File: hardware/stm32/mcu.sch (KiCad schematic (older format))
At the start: 13 parts, among them J1 LCD, J2 SD Card, J3 Radio, J4 Inside, J5 Outside, U1 PC817, U3 bluepill, U4 PC817

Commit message: bluepill Schematics 0.99
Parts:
- removed R3: R_Small, Resistors_SMD:R_0603_HandSoldering, symbol R_Small
- added C10, C4, C5, C6, C7: 100n, Capacitors_SMD:C_0805, symbol C_Small
- added C11, C8, C9: 10u, Capacitors_Tantalum_SMD:CP_Tantalum_Case-A_EIA-3216-18_Reflow, symbol CP_Small
- added J15: Screw_Terminal_01x02, TerminalBlock:TerminalBlock_bornier-2_P5.08mm, symbol Screw_Terminal_01x02
- added J16: Conn_01x02_Male, Pin_Headers:Pin_Header_Straight_1x02_Pitch2.54mm, symbol Conn_01x02_Male
- added J17: ESP-01, Socket_Strips:Socket_Strip_Straight_2x04_Pitch2.54mm, symbol Conn_02x04_Odd_Even
- added J18: USART1, Pin_Headers:Pin_Header_Straight_1x04_Pitch2.54mm, symbol Conn_01x04
- added J19: Buttons, Pin_Headers:Pin_Header_Straight_1x05_Pitch2.54mm, symbol Conn_01x05
- added R10, R11, R12, R6, R7, R8, R9: 470, Resistors_SMD:R_0603_HandSoldering, symbol R_Small
- added U12: LM1117-3.3, TO_SOT_Packages_SMD:SOT-223, symbol LM1117-3.3
- R1, R2: value R_Small -> 4.7k
- R4, R5: value R_Small -> 470
- U1, U4: footprint Housings_SSOP:SOP-4_3.8x4.1mm_Pitch2.54mm -> Housings_DIP:DIP-4_W7.62mm_LongPads
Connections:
- net +3V3: now also J2.6 (Pin_6), C10.1, C11.1, C7.1, C9.1, J17.3 (Pin_3), J17.4 (Pin_4), J17.5 (Pin_5), J17.6 (Pin_6), J17.8 (Pin_8), J18.4 (Pin_4), U12.2 (VO), U12.4 (VO)
- net +5V: now also C4.1, C5.1, C6.1, C8.1, J15.1 (Pin_1), J16.2 (Pin_2), U12.3 (VI); no longer J2.6 (Pin_6), U3.18 (5V)
- net GND: now also C10.2, C11.2, C4.2, C5.2, C6.2, C7.2, C8.2, C9.2, J15.2 (Pin_2), J17.1 (Pin_1), J18.1 (Pin_1), J19.5 (Pin_5), U12.1 (GND/ADJ)
- net IG: now also R12.2; no longer U3.25 (PA0)
- net IR: now also R10.2; no longer U3.27 (PA2)
- net IY: now also R11.2; no longer U3.26 (PA1)
- net LOOP_I: now also U3.4 (PB15); no longer U3.35 (PB10)
- net LOOP_O: now also U3.3 (PB14); no longer U3.36 (PB11)
- net OG: now also R9.2; no longer U3.28 (PA3)
- net OR: now also R7.2; no longer U3.34 (PB1)
- net OY: now also R8.2; no longer U3.33 (PB0)
- net at U3.1 (PB12): now also R6.2
- net BTN4: now reaches U3.10 (PA15)
- net BTN4: now also J19.4 (Pin_4)
- net TX1: now reaches U3.14 (PB6)
- net TX1: now also J18.3 (Pin_3)
- net RX1: now reaches U3.15 (PB7)
- net RX1: now also J18.2 (Pin_2)
- net BTN1: now reaches U3.7 (PA10)
- net BTN1: now also J19.1 (Pin_1)
- net BTN2: now reaches U3.8 (PA11)
- net BTN2: now also J19.2 (Pin_2)
- net BTN3: now reaches U3.9 (PA12)
- net BTN3: now also J19.3 (Pin_3)
- new net: J16.1 (Pin_1), U3.18 (5V)
- new net: R12.1, U3.25 (PA0)
- new net: R11.1, U3.26 (PA1)
- new net: R10.1, U3.27 (PA2)
- new net: R9.1, U3.28 (PA3)
- new net: R8.1, U3.33 (PB0)
- new net: R7.1, U3.34 (PB1)
- new net ESP_RX: J17.7 (Pin_7), U3.35 (PB10)
- new net ESP_TX: J17.2 (Pin_2), U3.36 (PB11)
- new net OPEN: R6.1
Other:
- moved on the sheet: J2

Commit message: bluepill PCB progress
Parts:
- added C12, C13: 100n, Capacitors_SMD:C_0805, symbol C_Small
- J15: value Screw_Terminal_01x02 -> +5V
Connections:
- net +3V3: now also C12.1, C13.1
- net +5V: now also J15.2 (Pin_2); no longer J15.1 (Pin_1)
- net GND: now also J15.1 (Pin_1), C12.2, C13.2; no longer J15.2 (Pin_2)
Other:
- moved on the sheet: C11, C9
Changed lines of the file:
@@
 $EndComp
 $Comp
-L +3.3V #PWR15
+L +3.3V #PWR09
 U 1 1 5A5F315E
 P 4600 2650
-F 0 "#PWR15" H 4600 2500 50  0001 C CNN
+F 0 "#PWR09" H 4600 2500 50  0001 C CNN
 F 1 "+3.3V" H 4600 2790 50  0000 C CNN
 F 2 "" H 4600 2650 50  0001 C CNN
@@
 $EndComp
 $Comp
-L GND #PWR18
+L GND #PWR010
 U 1 1 5A5F3165
 P 4700 5050
-F 0 "#PWR18" H 4700 4800 50  0001 C CNN
+F 0 "#PWR010" H 4700 4800 50  0001 C CNN
 F 1 "GND" H 4700 4900 50  0000 C CNN
 F 2 "" H 4700 5050 50  0001 C CNN
@@
 $EndComp
 $Comp
-L +3.3V #PWR19
+L +3.3V #PWR011
 U 1 1 5A5F316F
 P 6150 2650
-F 0 "#PWR19" H 6150 2500 50  0001 C CNN
+F 0 "#PWR011" H 6150 2500 50  0001 C CNN
 F 1 "+3.3V" H 6150 2790 50  0000 C CNN
 F 2 "" H 6150 2650 50  0001 C CNN
@@
 $EndComp
 $Comp
-L GND #PWR20
+L GND #PWR012
 U 1 1 5A5F317B
 P 6200 5050
-F 0 "#PWR20" H 6200 4800 50  0001 C CNN
+F 0 "#PWR012" H 6200 4800 50  0001 C CNN
 F 1 "GND" H 6200 4900 50  0000 C CNN
 F 2 "" H 6200 5050 50  0001 C CNN
@@
 $EndComp
 $Comp
-L +5V #PWR14
+L +5V #PWR013
 U 1 1 5A5F3181
 P 4500 4050
-F 0 "#PWR14" H 4500 3900 50  0001 C CNN
+F 0 "#PWR013" H 4500 3900 50  0001 C CNN
 F 1 "+5V" H 4500 4190 50  0000 C CNN
 F 2 "" H 4500 4050 50  0001 C CNN
@@
 $EndComp
 $Comp
-L GND #PWR12
+L GND #PWR014
 U 1 1 5A5F4705
 P 3850 5050
-F 0 "#PWR12" H 3850 4800 50  0001 C CNN
+F 0 "#PWR014" H 3850 4800 50  0001 C CNN
 F 1 "GND" H 3850 4900 50  0000 C CNN
 F 2 "" H 3850 5050 50  0001 C CNN
@@
 $EndComp
 $Comp
-L +5V #PWR11
+L +5V #PWR015
 U 1 1 5A5F5C21
 P 3850 2650
-F 0 "#PWR11" H 3850 2500 50  0001 C CNN
+F 0 "#PWR015" H 3850 2500 50  0001 C CNN
 F 1 "+5V" H 3850 2790 50  0000 C CNN
 F 2 "" H 3850 2650 50  0001 C CNN
@@
 CS
 $Comp
-L GND #PWR22
+L GND #PWR016
 U 1 1 5A5F62DE
 P 7050 3650
-F 0 "#PWR22" H 7050 3400 50  0001 C CNN
+F 0 "#PWR016" H 7050 3400 50  0001 C CNN
 F 1 "GND" H 7050 3500 50  0000 C CNN
 F 2 "" H 7050 3650 50  0001 C CNN
@@
 $EndComp
 $Comp
-L GND #PWR30
+L GND #PWR017
 U 1 1 5A5F7A2A
 P 9050 3700
-F 0 "#PWR30" H 9050 3450 50  0001 C CNN
+F 0 "#PWR017" H 9050 3450 50  0001 C CNN
 F 1 "GND" H 9050 3550 50  0000 C CNN
 F 2 "" H 9050 3700 50  0001 C CNN
@@
 $EndComp
 $Comp
-L +3.3V #PWR24
+L +3.3V #PWR018
 U 1 1 5A5F7B0F
 P 8000 2700
-F 0 "#PWR24" H 8000 2550 50  0001 C CNN
+F 0 "#PWR018" H 8000 2550 50  0001 C CNN
 F 1 "+3.3V" H 8000 2840 50  0000 C CNN
 F 2 "" H 8000 2700 50  0001 C CNN
@@
 Connection ~ 3250 1700
 $Comp
-L +5V #PWR9
+L +5V #PWR019
 U 1 1 5A60590D
 P 3250 1600
-F 0 "#PWR9" H 3250 1450 50  0001 C CNN
+F 0 "#PWR019" H 3250 1450 50  0001 C CNN
 F 1 "+5V" H 3250 1740 50  0000 C CNN
 F 2 "" H 3250 1600 50  0001 C CNN
@@
 $EndComp
 $Comp
-L +3.3V #PWR16
+L +3.3V #PWR020
 U 1 1 5A605990
 P 4700 1600
-F 0 "#PWR16" H 4700 1450 50  0001 C CNN
+F 0 "#PWR020" H 4700 1450 50  0001 C CNN
 F 1 "+3.3V" H 4700 1740 50  0000 C CNN
 F 2 "" H 4700 1600 50  0001 C CNN
@@
 $EndComp
 $Comp
-L GND #PWR10
+L GND #PWR021
 U 1 1 5A6059E3
 P 3250 2100
-F 0 "#PWR10" H 3250 1850 50  0001 C CNN
+F 0 "#PWR021" H 3250 1850 50  0001 C CNN
 F 1 "GND" H 3250 1950 50  0000 C CNN
 F 2 "" H 3250 2100 50  0001 C CNN
@@
 L Screw_Terminal_01x02 J15
 U 1 1 5A606802
-P 2600 1800
-F 0 "J15" H 2600 1900 50  0000 C CNN
-F 1 "Screw_Terminal_01x02" H 2600 1600 50  0001 C CNN
-F 2 "TerminalBlock:TerminalBlock_bornier-2_P5.08mm" H 2600 1800 50  0001 C CNN
-F 3 "" H 2600 1800 50  0001 C CNN
-	1    2600 1800
-	-1   0    0    -1
+P 2600 1900
+F 0 "J15" H 2600 2000 50  0000 C CNN
+F 1 "+5V" H 2600 1700 50  0000 C CNN
+F 2 "TerminalBlock:TerminalBlock_bornier-2_P5.08mm" H 2600 1900 50  0001 C CNN
+F 3 "" H 2600 1900 50  0001 C CNN
+	1    2600 1900
+	-1   0    0    1
 $EndComp
 Wire Wire Line
@@
 Connection ~ 3050 1700
 $Comp
-L +3.3V #PWR21
+L +3.3V #PWR022
 U 1 1 5A606B55
 P 7050 2650
-F 0 "#PWR21" H 7050 2500 50  0001 C CNN
+F 0 "#PWR022" H 7050 2500 50  0001 C CNN
 F 1 "+3.3V" H 7050 2790 50  0000 C CNN
 F 2 "" H 7050 2650 50  0001 C CNN
@@
 Connection ~ 3450 2000
 $Comp
-L GND #PWR13
+L GND #PWR023
 U 1 1 5A6076E6
 P 4100 2100
-F 0 "#PWR13" H 4100 1850 50  0001 C CNN
+F 0 "#PWR023" H 4100 1850 50  0001 C CNN
 F 1 "GND" H 4100 1950 50  0000 C CNN
 F 2 "" H 4100 2100 50  0001 C CNN
@@
 	4100 2000 4100 2100
 Wire Wire Line
-	4400 1700 5100 1700
+	4400 1700 5500 1700
 Wire Wire Line
 	4500 1700 4500 1750
@@
 	4500 1950 4500 2000
 $Comp
-L GND #PWR17
+L GND #PWR024
 U 1 1 5A607B90
 P 4700 2100
-F 0 "#PWR17" H 4700 1850 50  0001 C CNN
+F 0 "#PWR024" H 4700 1850 50  0001 C CNN
 F 1 "GND" H 4700 1950 50  0000 C CNN
 F 2 "" H 4700 2100 50  0001 C CNN
@@
 L CP_Small C9
 U 1 1 5A607922
-P 4900 1850
-F 0 "C9" H 4910 1920 50  0000 L CNN
-F 1 "10u" H 4910 1770 50  0000 L CNN
-F 2 "Capacitors_Tantalum_SMD:CP_Tantalum_Case-A_EIA-3216-18_Reflow" H 4900 1850 50  0001 C CNN
-F 3 "" H 4900 1850 50  0001 C CNN
-	1    4900 1850
+P 5300 1850
+F 0 "C9" H 5310 1920 50  0000 L CNN
+F 1 "10u" H 5310 1770 50  0000 L CNN
+F 2 "Capacitors_Tantalum_SMD:CP_Tantalum_Case-A_EIA-3216-18_Reflow" H 5300 1850 50  0001 C CNN
+F 3 "" H 5300 1850 50  0001 C CNN
+	1    5300 1850
 	1    0    0    -1
 $EndComp
@@
 $EndComp
 Wire Wire Line
-	4900 1700 4900 1750
-Wire Wire Line
-	4500 2000 5100 2000
-Wire Wire Line
-	4900 2000 4900 1950
+	5300 1700 5300 1750
+Wire Wire Line
+	4500 2000 5500 2000
+Wire Wire Line
+	5300 2000 5300 1950
 Wire Wire Line
 	4700 1950 4700 2100
@@
 $EndComp
 $Comp
-L GND #PWR29
+L GND #PWR025
 U 1 1 5A60891B
 P 9000 4700
-F 0 "#PWR29" H 9000 4450 50  0001 C CNN
+F 0 "#PWR025" H 9000 4450 50  0001 C CNN
 F 1 "GND" H 9000 4550 50  0000 C CNN
 F 2 "" H 9000 4700 50  0001 C CNN
@@
 $EndComp
 $Comp
-L +3.3V #PWR28
+L +3.3V #PWR026
 U 1 1 5A608983
 P 9000 4200
-F 0 "#PWR28" H 9000 4050 50  0001 C CNN
+F 0 "#PWR026" H 9000 4050 50  0001 C CNN
 F 1 "+3.3V" H 9000 4340 50  0000 C CNN
 F 2 "" H 9000 4200 50  0001 C CNN
@@
 $EndComp
 $Comp
-L GND #PWR26
+L GND #PWR027
 U 1 1 5A609212
 P 8450 4700
-F 0 "#PWR26" H 8450 4450 50  0001 C CNN
+F 0 "#PWR027" H 8450 4450 50  0001 C CNN
 F 1 "GND" H 8450 4550 50  0000 C CNN
 F 2 "" H 8450 4700 50  0001 C CNN
@@
 	8450 4600 8450 4700
 $Comp
-L +3.3V #PWR23
+L +3.3V #PWR028
 U 1 1 5A609319
 P 7750 4150
-F 0 "#PWR23" H 7750 4000 50  0001 C CNN
+F 0 "#PWR028" H 7750 4000 50  0001 C CNN
 F 1 "+3.3V" H 7750 4290 50  0000 C CNN
 F 2 "" H 7750 4150 50  0001 C CNN
@@
 Connection ~ 7750 4400
 $Comp
-L +3.3V #PWR25
+L +3.3V #PWR029
 U 1 1 5A609773
 P 8450 4150
-F 0 "#PWR25" H 8450 4000 50  0001 C CNN
+F 0 "#PWR029" H 8450 4000 50  0001 C CNN
 F 1 "+3.3V" H 8450 4290 50  0000 C CNN
 F 2 "" H 8450 4150 50  0001 C CNN
@@
 L CP_Small C11
 U 1 1 5A609B69
-P 5100 1850
-F 0 "C11" H 5110 1920 50  0000 L CNN
-F 1 "10u" H 5110 1770 50  0000 L CNN
-F 2 "Capacitors_Tantalum_SMD:CP_Tantalum_Case-A_EIA-3216-18_Reflow" H 5100 1850 50  0001 C CNN
-F 3 "" H 5100 1850 50  0001 C CNN
-	1    5100 1850
-	1    0    0    -1
-$EndComp
-Wire Wire Line
-	5100 1700 5100 1750
-Connection ~ 4900 1700
-Wire Wire Line
-	5100 2000 5100 1950
-Connection ~ 4900 2000
+P 5500 1850
+F 0 "C11" H 5510 1920 50  0000 L CNN
+F 1 "10u" H 5510 1770 50  0000 L CNN
+F 2 "Capacitors_Tantalum_SMD:CP_Tantalum_Case-A_EIA-3216-18_Reflow" H 5500 1850 50  0001 C CNN
+F 3 "" H 5500 1850 50  0001 C CNN
+	1    5500 1850
+	1    0    0    -1
+$EndComp
+Wire Wire Line
+	5500 1700 5500 1750
+Connection ~ 5300 1700
+Wire Wire Line
+	5500 2000 5500 1950
+Connection ~ 5300 2000
 Text Label 4800 3650 2    60   ~ 0
 BTN1
@@
 $EndComp
 $Comp
-L GND #PWR27
+L GND #PWR030
 U 1 1 5A60ABBB
 P 9000 2450
-F 0 "#PWR27" H 9000 2200 50  0001 C CNN
+F 0 "#PWR030" H 9000 2200 50  0001 C CNN
 F 1 "GND" H 9000 2300 50  0000 C CNN
 F 2 "" H 9000 2450 50  0001 C CNN
@@
 Text Label 9100 2250 2    60   ~ 0
 BTN4
+$Comp
+L C_Small C12
+U 1 1 5A6204B4
+P 4900 1850
+F 0 "C12" H 4910 1920 50  0000 L CNN
+F 1 "100n" H 4910 1770 50  0000 L CNN
+F 2 "Capacitors_SMD:C_0805" H 4900 1850 50  0001 C CNN
+F 3 "" H 4900 1850 50  0001 C CNN
+	1    4900 1850
+	1    0    0    -1
+$EndComp
+$Comp
+L C_Small C13
+U 1 1 5A620536
+P 5100 1850
+F 0 "C13" H 5110 1920 50  0000 L CNN
+F 1 "100n" H 5110 1770 50  0000 L CNN
+F 2 "Capacitors_SMD:C_0805" H 5100 1850 50  0001 C CNN
+F 3 "" H 5100 1850 50  0001 C CNN
+	1    5100 1850
+	1    0    0    -1
+$EndComp
+Wire Wire Line
+	4900 1700 4900 1750
+Connection ~ 4900 1700
+Wire Wire Line
+	5100 1700 5100 1750
+Connection ~ 5100 1700
+Wire Wire Line
+	4900 1950 4900 2000
+Connection ~ 4900 2000
+Wire Wire Line
+	5100 1950 5100 2000
+Connection ~ 5100 2000
 $EndSCHEMATC

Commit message: bluepill: PCB 0.9
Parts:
- removed C13: 100n, Capacitors_SMD:C_0805, symbol C_Small
- removed J18: USART1, Pin_Headers:Pin_Header_Straight_1x04_Pitch2.54mm, symbol Conn_01x04
- removed J4: Inside, Pin_Headers:Pin_Header_Straight_1x03_Pitch2.54mm, symbol Conn_01x03
- removed J5: Outside, Pin_Headers:Pin_Header_Straight_1x03_Pitch2.54mm, symbol Conn_01x03
- added J18: USART1, Pin_Headers:Pin_Header_Straight_1x03_Pitch2.54mm, symbol Conn_01x03
- added J4: Outer, Pin_Headers:Pin_Header_Straight_1x02_Pitch2.54mm, symbol Conn_01x02
- added J5: Inner, Pin_Headers:Pin_Header_Straight_1x02_Pitch2.54mm, symbol Conn_01x02
- added R3: 1.8k, Resistors_SMD:R_0603_HandSoldering, symbol R_Small
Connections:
- net +3V3: now also R3.1
- net BTN1: now also U3.10 (PA15); no longer U3.7 (PA10)
- net BTN2: now also U3.11 (PB3); no longer U3.8 (PA11)
- net BTN3: now also U3.12 (PB4); no longer U3.9 (PA12)
- net BTN4: now also U3.13 (PB5); no longer U3.10 (PA15)
- net GND: now also J18.1 (Pin_1)
- net RX1: now also J18.2 (Pin_2)
- net TX1: now also J18.3 (Pin_3)
- net at R4.2: now also J4.1 (Pin_1)
- net at U1.2: now also J4.2 (Pin_2)
- net at R5.2: now also J5.1 (Pin_1)
- net at U4.2: now also J5.2 (Pin_2)
- new net USB+: R3.2, U3.9 (PA12)
- new net USB-: U3.8 (PA11)
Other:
- moved on the sheet: C11, C9

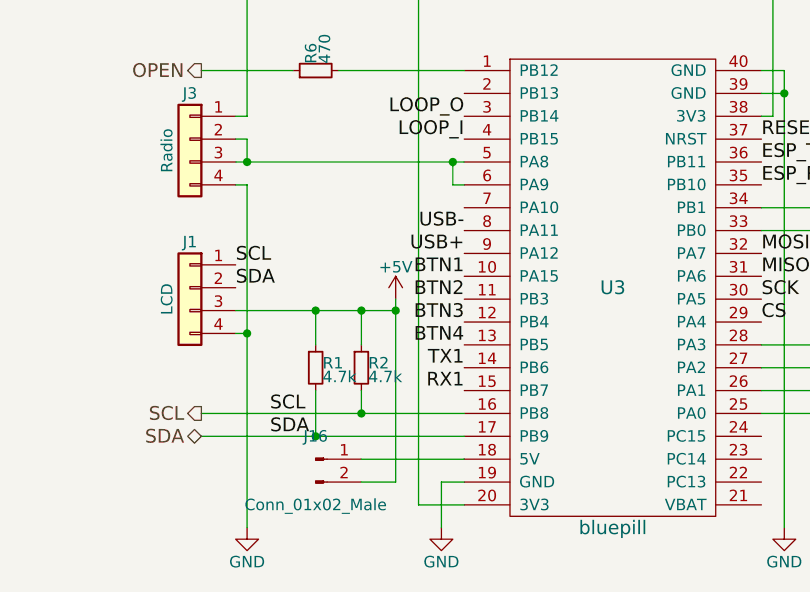
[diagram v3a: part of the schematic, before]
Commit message: bluepill PCB: SD Card socket turned around
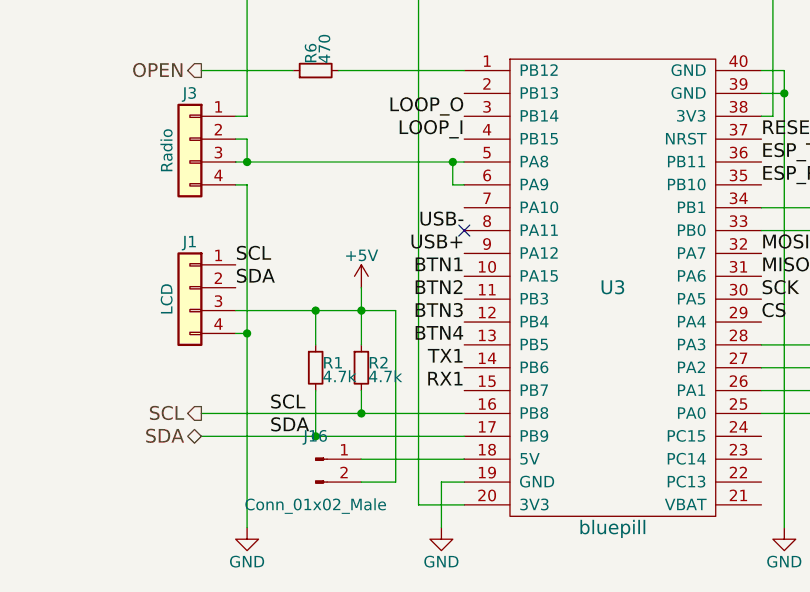
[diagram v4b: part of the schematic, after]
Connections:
- no-connect marks 0 -> 1
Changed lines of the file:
@@
-	1    0    0    -1
-$EndComp
-$Comp
-L +5V #PWR12
-U 1 1 5A5F3181
-P 4500 4050
-F 0 "#PWR12" H 4500 3900 50  0001 C CNN
-F 1 "+5V" H 4500 4190 50  0000 C CNN
-F 2 "" H 4500 4050 50  0001 C CNN
-F 3 "" H 4500 4050 50  0001 C CNN
-	1    4500 4050
 	1    0    0    -1
 $EndComp
@@
 	3800 4100 4500 4100
 Wire Wire Line
-	4350 4250 4350 4100
+	4350 4000 4350 4250
 Connection ~ 4350 4100
 Connection ~ 4150 4100
@@
 	4800 3550 4750 3550
 Wire Wire Line
-	4750 3450 4750 3550
+	4750 3550 4750 3450
 Wire Wire Line
 	3800 3450 4800 3450
@@
 $EndComp
 Wire Wire Line
-	4500 4050 4500 4850
+	4500 4100 4500 4850
 $Comp
 L Conn_01x02_Male J16
@@
 Wire Wire Line
 	4500 4850 4350 4850
-Connection ~ 4500 4100
 $Comp
 L CP_Small C8
@@
 Text Label 7600 5050 0    60   ~ 0
 USB+
+$Comp
+L +5V #PWR12
+U 1 1 5A5F3181
+P 4350 4000
+F 0 "#PWR12" H 4350 3850 50  0001 C CNN
+F 1 "+5V" H 4350 4140 50  0000 C CNN
+F 2 "" H 4350 4000 50  0001 C CNN
+F 3 "" H 4350 4000 50  0001 C CNN
+	1    4350 4000
+	1    0    0    -1
+$EndComp
+NoConn ~ 4800 3750
 $EndSCHEMATC
